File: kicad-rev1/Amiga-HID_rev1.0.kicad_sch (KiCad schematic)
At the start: 56 parts, among them J1 USB-A Host, J2 JST-XH-5A, J3 OLED I2C, J4 Reserve 3V3+GP+GND+VSYS, J5 JST-SH-3 SWD, J6 JST-SH-3 UART, J7 Conn_01x06_Pin, SW1 SW_Push, SW2 SW_Push, U1 USBLC6-2SC6, U2 AMS1117-3.3, U3 W25Q128JVS, U4 RP2350_60QFN, U5 TXS0102DCUR, Y1 12MHz_3225_8pF

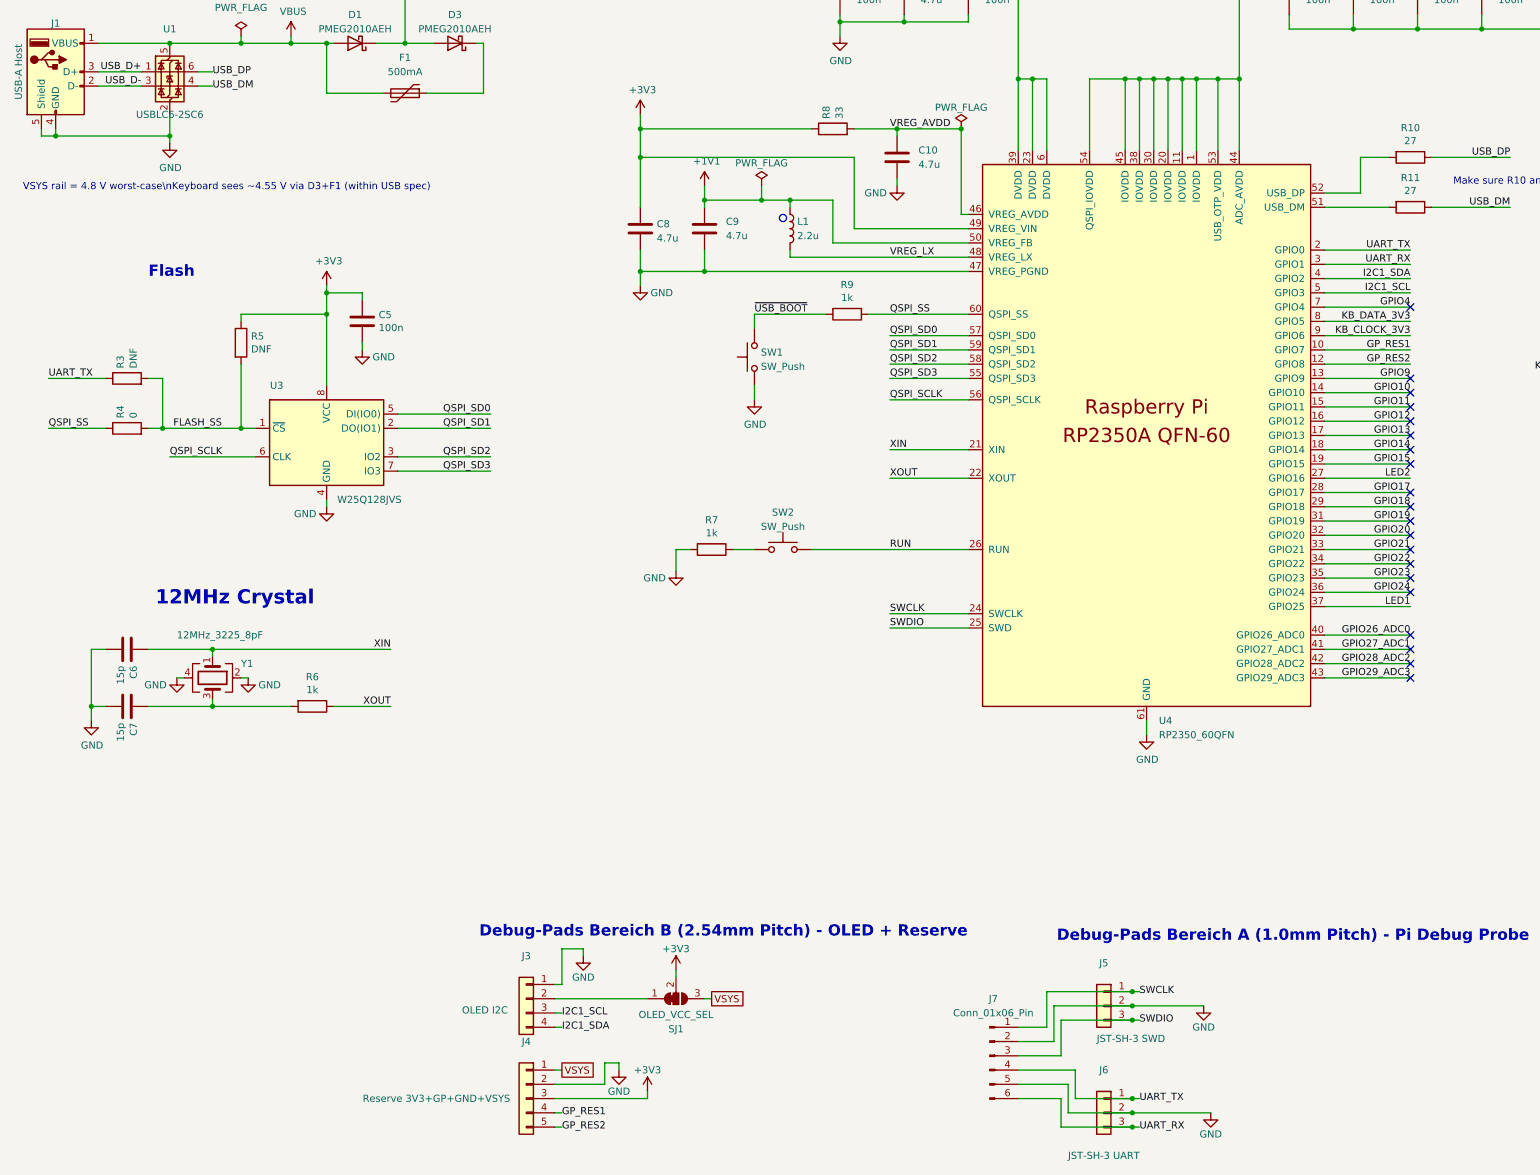
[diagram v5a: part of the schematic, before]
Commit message: Wiederstände überarbeitet
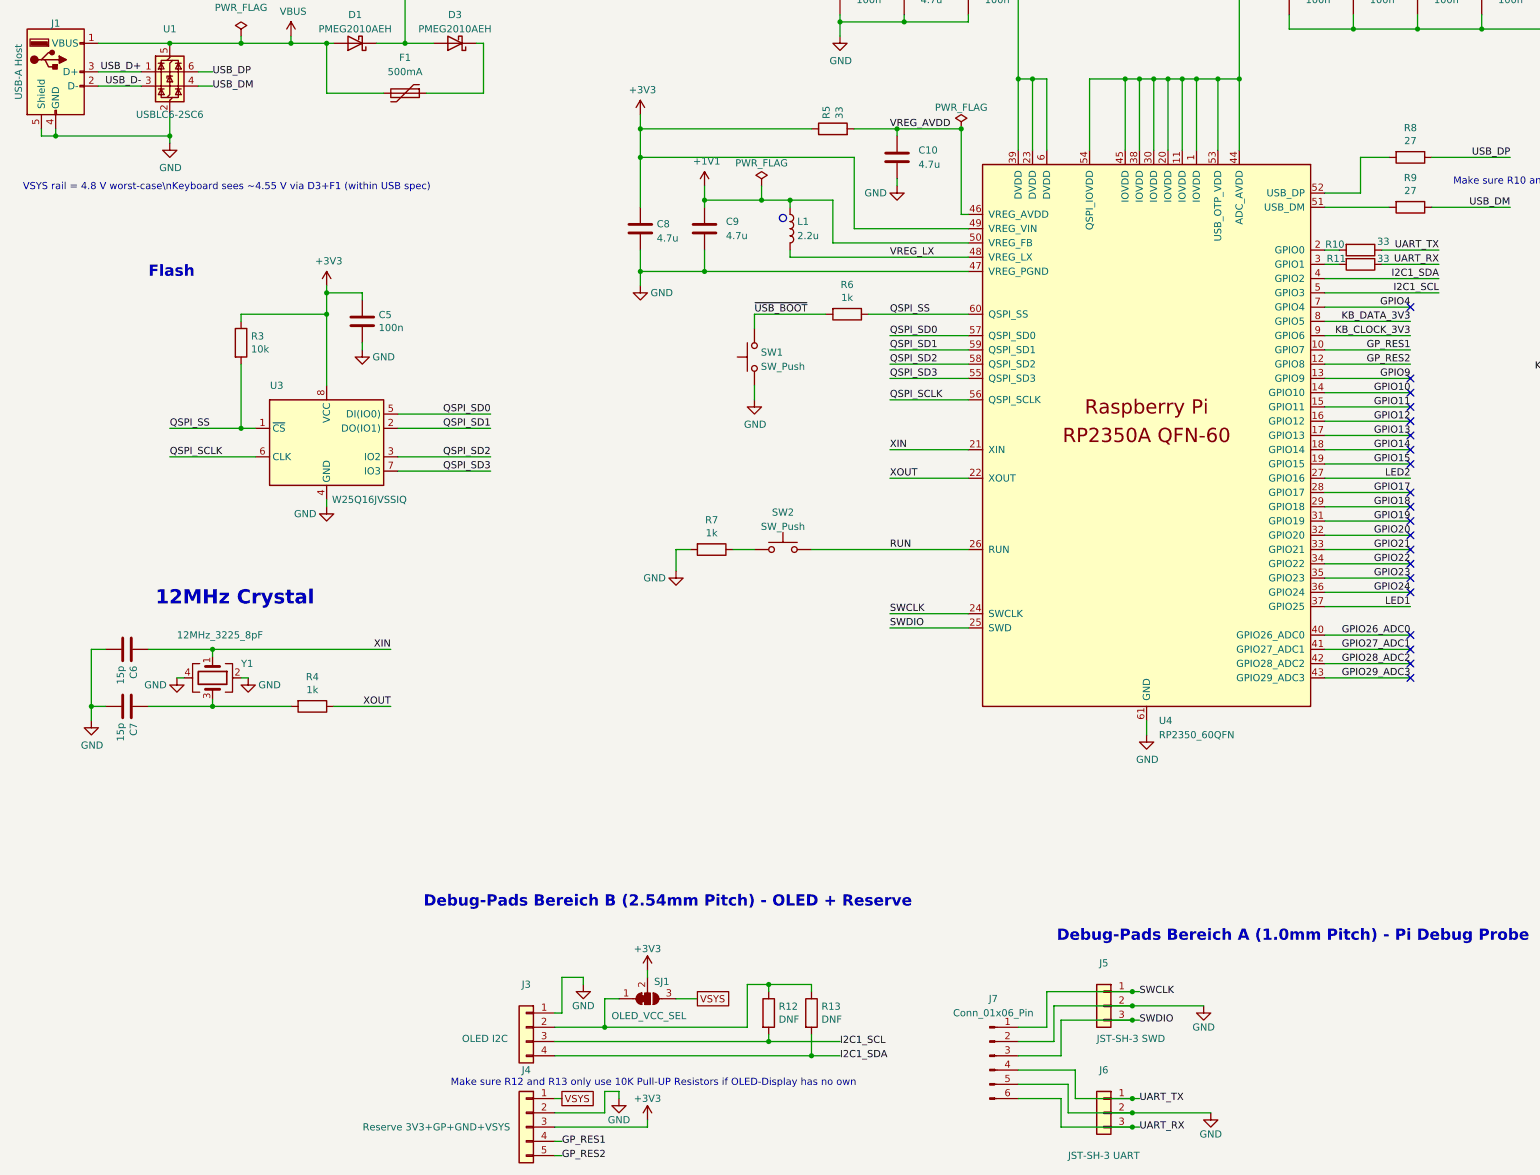
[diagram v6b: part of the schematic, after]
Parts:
- removed R3: DNF, Resistor_SMD:R_0402_1005Metric, symbol Device:R
- removed R4: 0, Resistor_SMD:R_0402_1005Metric, symbol Device:R
- added R10, R11: 33, Resistor_SMD:R_0402_1005Metric, symbol Device:R
- added R12, R13: DNF, Resistor_SMD:R_0402_1005Metric, symbol Device:R
- R3: renamed from R5; value DNF -> 10k
- U3: value W25Q128JVS -> W25Q16JVSSIQ
- renumbered R6 to R4, R8 to R5, R9 to R6, R10 to R8, R11 to R9
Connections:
- net FLASH_SS is gone; now on net QSPI_SS: R3.2, U3.1 (~{CS})
- net I2C1_SCL: now also R12.2
- net I2C1_SDA: now also R13.2
- net UART_RX: now also R11.1; no longer U4.3 (GPIO1)
- net UART_TX: now also R10.1; no longer U4.2 (GPIO0)
- net at J3.2 (Pin_2), SJ1.1 (A): now also R12.1, R13.1
- new net: R10.2, U4.2 (GPIO0)
- new net: R11.2, U4.3 (GPIO1)
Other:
- note added: "Make sure R12 and R13 only use 10K Pull-UP Resistors if OLED-Display has no own"
- moved on the sheet: J3, J4, SJ1
